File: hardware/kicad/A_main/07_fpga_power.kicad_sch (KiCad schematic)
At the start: 41 parts, among them J10 JTAG 2x3, SW1 PROG, U10 LFE5U-25F-7BG256I, U11 W25Q128JVSIQ

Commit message: Connect the pads that had no net
A symbol pin number must agree with the footprint pad number. If the
numbers do not agree, the net goes nowhere. The netlist removes it
and gives no message. ERC examines the schematic and sees a wire. DRC
does not count an unconnected pad as a violation. All three boards
showed zero ERC violations while 31 pads had no net.

Two of these faults stopped a board.

The footprint of the Ethernet PHY was for a different part. The
project used QFN-48 6x6 mm with 0.4 mm pitch. The RTL8211F(I)-CG is
WQFN-40-EP 5x5 mm. You cannot solder the part to that pad pattern.

The 25 MHz crystal had a 2-pin symbol on a 4-pad footprint. On a 3225
crystal the terminals are the diagonal pads 1 and 3. Pads 2 and 4 are
the metal can. XO went to pad 2. There was no crystal between XI and
XO, and thus neither PHY could make a clock.

The paddle of the AD9251 was pin 0 in the symbol and pad 65 in the
footprint. The paddle of the PE4312 was Pad against pad 21. The gas
discharge tubes had one electrode unconnected, because
Device:GDT_2Pin uses pins 1 and 3 but the varistor footprint uses
pads 1 and 2. A local footprint with pads 1 and 3 corrects this.

ped_denetim.py finds these faults on the board. yap.sh runs it before
the DSN export. The chain stops if a pad has no net.

The DSN export also changed. It declared In1 and In4 as power layers
but did not export the copper on them. The router thus believed that
the two ground planes were empty. It routed the 289 pins of GND as
traces on the signal layers. The planes now go out as conduction
areas.
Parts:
- C100, C104: footprint Capacitor_SMD:C_0603_1608Metric -> Capacitor_SMD:C_1206_3216Metric
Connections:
- net LED_RX: now reaches U10.R6 (D6/PB4B)
- no-connect marks 10 -> 9
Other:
- note added: "GUC SIRALAMASI — VCCIO ONCE, CEKIRDEK SONRA U1 (VIN -> +3V3) EN girise bagli, hep acik U8 (+3V3 -> +2V5 VCCAUX) U2 (+3V3 -> +1V1 VCC) EN = PG_3V3, 3.3 V oturunca kalkar yani +3V3 (VCCIO) -> +2V5 (VCCAUX) -> +1V1 (VCC) Bu sayfada once 'VCC once, VCCIO en son' yaziyordu; YANLISTI. Lattice ECP5 Hardware Checklist / sysIO Usage Guide: 'It is recommended that the I/O buffers be powered-up prior to the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"
- note removed: "GUC SIRALAMASI (Lattice: VCC once, VCCIO en son) U1 (+3V3) PG -> U2 (+1V1) EN 01_power'da zincirli +1V1 kalkar -> +2V5 VCCAUX -> +1V8 / +3V3 VCCIO Sira bozulursa girisler govde diyodundan besleme cekiyor: yuksek akim, en kotu halde latch-up."

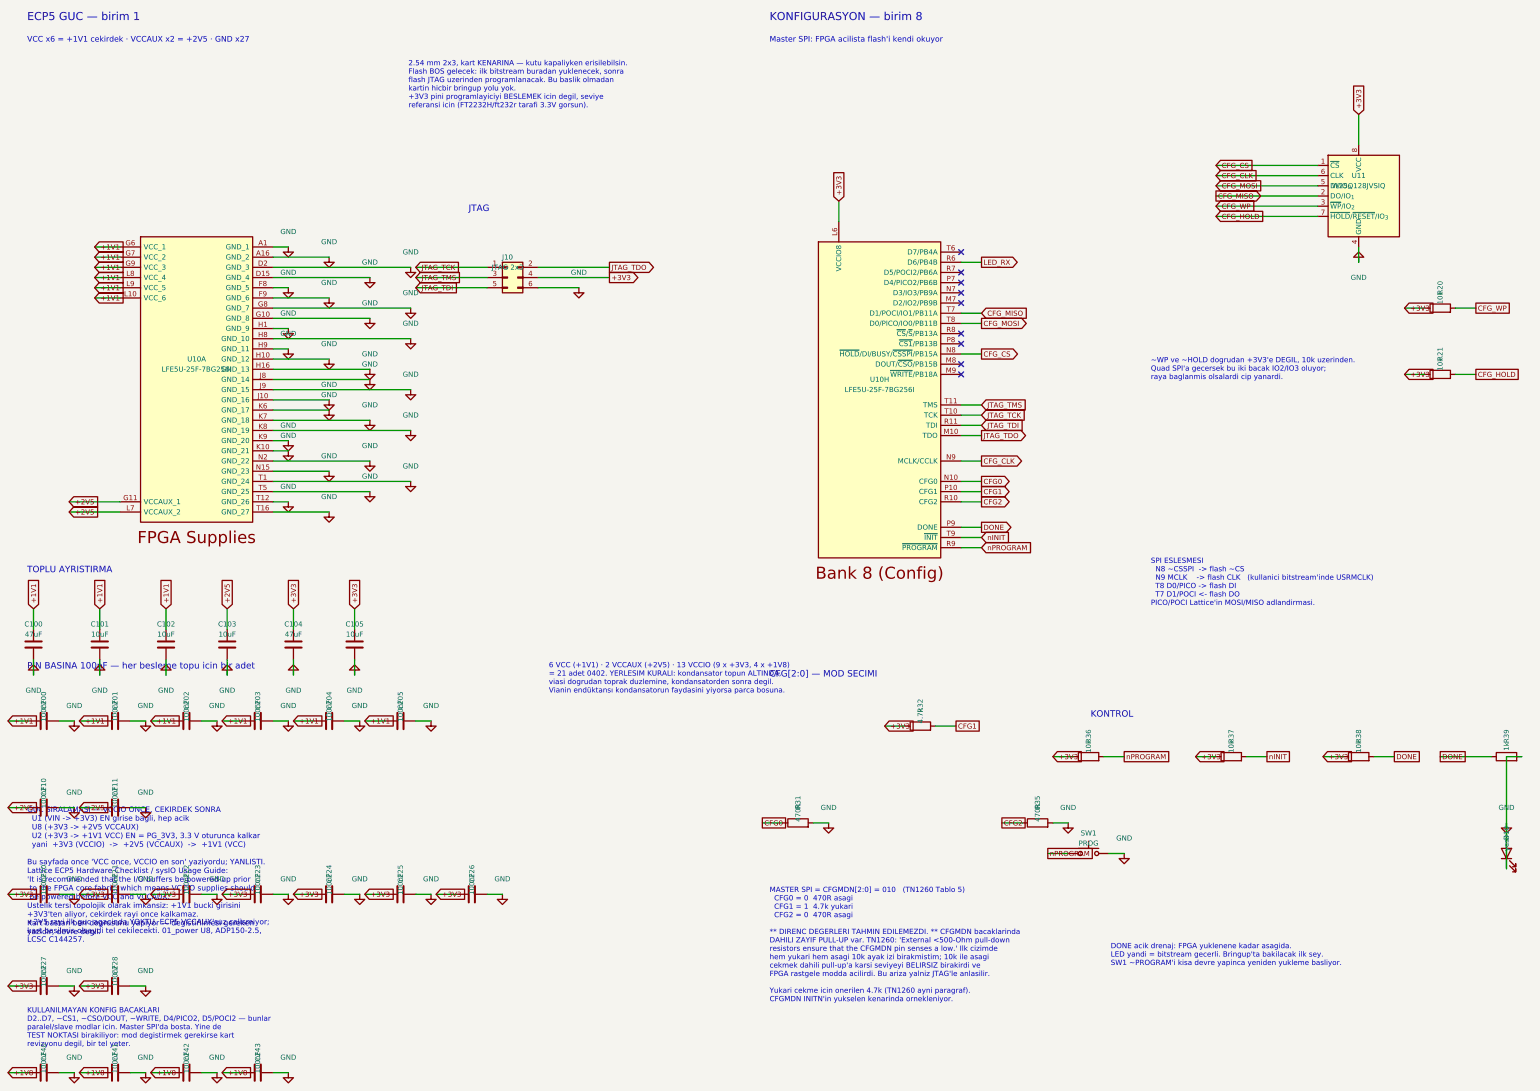
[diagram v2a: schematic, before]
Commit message: Correct the clearance test for the pre-routed traces
The clearance test used a circle for each pad. The radius was
max(width, height)/2. The corner of a rectangle is at
hypot(width, height)/2 from the center. The test thus made the pad
smaller than it is. On the 2.5 x 4.5 mm gate pad of a TO-247 the
difference is 2.250 mm against 2.574 mm.

The DRN_A trace was on the gate pad of Q10 with an overlap of 35 um.
This is a short circuit between the 50 V drain rail and the gate of a
100 W device. The search that finds the tee offset accepted this
route. The overlap is at a corner and 35 um wide. You cannot see it
on a plot.

The test now uses the real shape of the pad and the collision test of
pcbnew. It also uses the 300 um clearance and not only an overlap. A
trace that is 50 um from a pad is also not possible to manufacture.

Board D was built again. No trace is below 300 um and the smallest
gap is 0.537 mm. Boards A and C were correct.
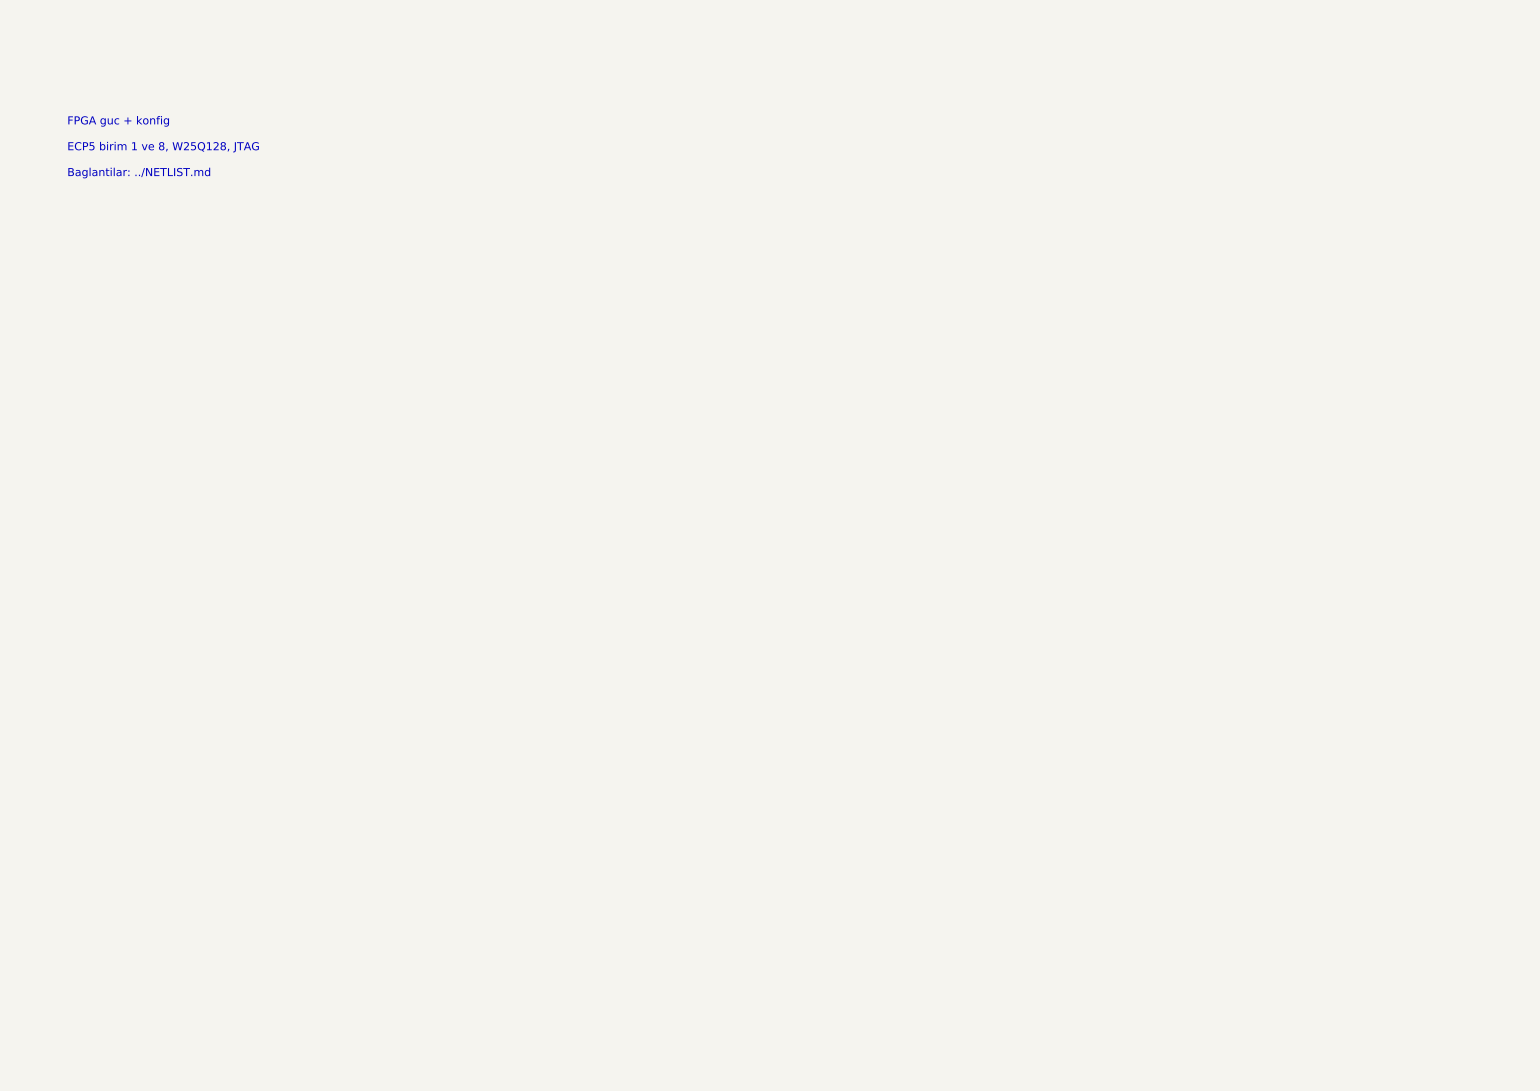
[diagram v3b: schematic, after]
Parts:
- removed C100, C104: 47uF, Capacitor_SMD:C_1206_3216Metric, symbol Device:C
- removed C101, C102, C103, C105: 10uF, Capacitor_SMD:C_0603_1608Metric, symbol Device:C
- removed C200, C201, C202, C203, C204, C205, C210, C211, C220, C221, C222, C223, C224, C225, C226, C227, C228, C240, C241, C242, C243: 100nF, Capacitor_SMD:C_0402_1005Metric, symbol Device:C
- removed D10: yesil, LED_SMD:LED_0603_1608Metric, symbol Device:LED
- removed J10: JTAG 2x3, Connector_PinHeader_2.54mm:PinHeader_2x03_P2.54mm_Vertical, symbol Connector_Generic:Conn_02x03_Odd_Even
- removed R20, R21, R36, R37, R38: 10k, Resistor_SMD:R_0603_1608Metric, symbol Device:R
- removed R31, R35: 470R, Resistor_SMD:R_0603_1608Metric, symbol Device:R
- removed R32: 4.7k, Resistor_SMD:R_0603_1608Metric, symbol Device:R
- removed R39: 1k, Resistor_SMD:R_0603_1608Metric, symbol Device:R
- removed SW1: PROG, Button_Switch_SMD:SW_SPST_TL3342, symbol Switch:SW_Push
- removed U10: LFE5U-25F-7BG256I, Package_BGA:BGA-256_14.0x14.0mm_Layout16x16_P0.8mm_Ball0.45mm_Pad0.32mm_NSMD, symbol dogrudan-sdr:ECP5-BGA256
- removed U11: W25Q128JVSIQ, Package_SO:SOIC-8_5.3x5.3mm_P1.27mm, symbol Memory_Flash:W25Q128JVS
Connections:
- no-connect marks 9 -> 0
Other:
- note added: "FPGA guc + konfig ECP5 birim 1 ve 8, W25Q128, JTAG Baglantilar: ../NETLIST.md"
- note removed: "+2V5 rayi ilk guc agacinda YOKTU. ECP5 VCCAUX'suz calismiyor; kart basilmis olsaydi tel cekilecekti. 01_power U8, ADP150-2.5, LCSC C144257."
- note removed: "2.54 mm 2x3, kart KENARINA — kutu kapaliyken erisilebilsin. Flash BOS gelecek: ilk bitstream buradan yuklenecek, sonra flash JTAG uzerinden programlanacak. Bu baslik olmadan kartin hicbir bringup yolu yok. +3V3 pini programlayiciyi BESLEMEK icin degil, seviye referansi icin (FT2232H/ft232r tarafi 3.3V gorsun)."
- note removed: "6 VCC (+1V1) · 2 VCCAUX (+2V5) · 13 VCCIO (9 x +3V3, 4 x +1V8) = 21 adet 0402. YERLESIM KURALI: kondansator topun ALTINDA, viasi dogrudan toprak duzlemine, kondansatorden sonra degil. Vianin endüktansı kondansatorun faydasini yiyorsa parca bosuna."
- note removed: "CFG[2:0] — MOD SECIMI"
- note removed: "DONE acik drenaj: FPGA yuklenene kadar asagida. LED yandi = bitstream gecerli. Bringup'ta bakilacak ilk sey. SW1 ~PROGRAM'i kisa devre yapinca yeniden yukleme basliyor."
- note removed: "ECP5 GUC — birim 1"
- note removed: "GUC SIRALAMASI — VCCIO ONCE, CEKIRDEK SONRA U1 (VIN -> +3V3) EN girise bagli, hep acik U8 (+3V3 -> +2V5 VCCAUX) U2 (+3V3 -> +1V1 VCC) EN = PG_3V3, 3.3 V oturunca kalkar yani +3V3 (VCCIO) -> +2V5 (VCCAUX) -> +1V1 (VCC) Bu sayfada once 'VCC once, VCCIO en son' yaziyordu; YANLISTI. Lattice ECP5 Hardware Checklist / sysIO Usage Guide: 'It is recommended that the I/O buffers be powered-up prior to the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"
- note removed: "JTAG"
- note removed: "KONFIGURASYON — birim 8"
- note removed: "KONTROL"
- note removed: "KULLANILMAYAN KONFIG BACAKLARI D2..D7, ~CS1, ~CSO/DOUT, ~WRITE, D4/PICO2, D5/POCI2 — bunlar paralel/slave modlar icin. Master SPI'da bosta. Yine de TEST NOKTASI birakiliyor: mod degistirmek gerekirse kart revizyonu degil, bir tel yeter."
- note removed: "MASTER SPI = CFGMDN[2:0] = 010 (TN1260 Tablo 5) CFG0 = 0 470R asagi CFG1 = 1 4.7k yukari CFG2 = 0 470R asagi ** DIRENC DEGERLERI TAHMIN EDILEMEZDI. ** CFGMDN bacaklarinda DAHILI ZAYIF PULL-UP var. TN1260: 'External <500-Ohm pull-down resistors ensure that the CFGMDN pin senses a low.' Ilk cizimde hem yukari hem asagi 10k ayak izi birakmistim; 10k ile asagi cekmek dahili pull-up'a karsi seviyeyi B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"
- note removed: "Master SPI: FPGA acilista flash'i kendi okuyor"
- note removed: "PIN BASINA 100nF — her besleme topu icin bir adet"
- note removed: "SPI ESLESMESI N8 ~CSSPI -> flash ~CS N9 MCLK -> flash CLK (kullanici bitstream'inde USRMCLK) T8 D0/PICO -> flash DI T7 D1/POCI <- flash DO PICO/POCI Lattice'in MOSI/MISO adlandirmasi."
- note removed: "TOPLU AYRISTIRMA"
- note removed: "VCC x6 = +1V1 cekirdek · VCCAUX x2 = +2V5 · GND x27"
- note removed: "~WP ve ~HOLD dogrudan +3V3'e DEGIL, 10k uzerinden. Quad SPI'a gecersek bu iki bacak IO2/IO3 oluyor; raya baglanmis olsalardi cip yanardi."
- title: FPGA guc + konfigurasyon -> FPGA guc + konfig
